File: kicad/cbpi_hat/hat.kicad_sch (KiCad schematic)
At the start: 26 parts, among them J1 GPIO, J2 Screw_Terminal_01x02, U1 CAT24C256, U2 EUP3453WIR1

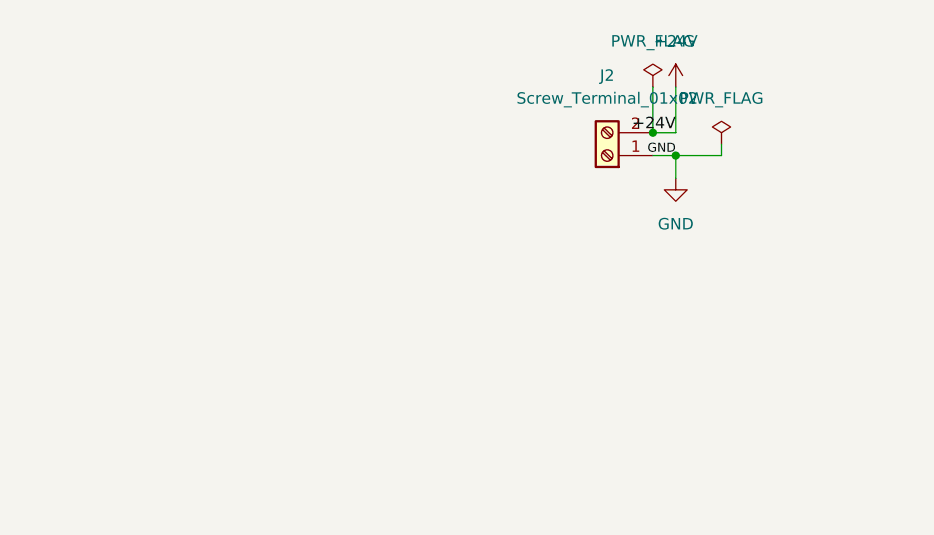
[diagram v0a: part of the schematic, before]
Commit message: The schematic should now have the current reverse polarity proection
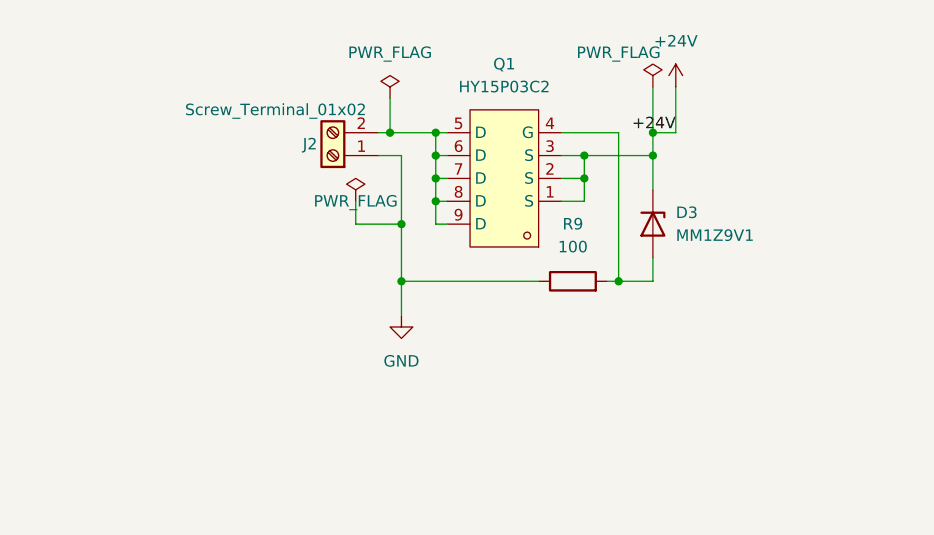
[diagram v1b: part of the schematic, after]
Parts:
- added D3: MM1Z9V1, symbol Device:D_Zener
- added Q1: HY15P03C2, hy15p03c2:DFN-8_L5.9-W5.2-P1.27-LS6.2-BL, symbol hy15p03c2:HY15P03C2
- added R9: 100, symbol Device:R
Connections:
- net +24V: now also D3.1 (K), Q1.1 (S), Q1.2 (S), Q1.3 (S); no longer J2.2 (Pin_2)
- net GND: now also R9.1
- new net: D3.2 (A), Q1.4 (G), R9.2
- new net: J2.2 (Pin_2), Q1.5 (D), Q1.6 (D), Q1.7 (D), Q1.8 (D), Q1.9 (D)
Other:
- moved on the sheet: J2

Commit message: Placed first components on board, no routing yet
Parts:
- D1: footprint Diode_SMD:D_SMC -> Diode_SMD:D_SMA
- D2: footprint smbj5:SMB_L4.6-W3.6-LS5.3-BI -> smbj5.0ca-tp:SMB_L4.6-W3.6-LS5.3-BI
- D3: footprint (none) -> Diode_SMD:D_SOD-123
- J2: footprint (none) -> TerminalBlock:TerminalBlock_Altech_AK300-2_P5.00mm
- R9: footprint (none) -> Resistor_SMD:R_01005_0402Metric
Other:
- note added: "Power In/ Reverse Polarity Protection"
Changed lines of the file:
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@@
+    (stroke (width 0) (type default) (color 0 0 0 0))
+  )
+  (polyline (pts (xy 292.1 12.7) (xy 292.1 53.34))
     (stroke (width 0) (type default) (color 0 0 0 0))
   )
@@
     (stroke (width 0) (type solid) (color 0 0 0 0))
   )
+  (polyline (pts (xy 359.41 12.7) (xy 359.41 53.34))
+    (stroke (width 0) (type default) (color 0 0 0 0))
+  )
   (wire (pts (xy 538.48 48.26) (xy 543.56 48.26))
     (stroke (width 0) (type default) (color 0 0 0 0))
@@
     (stroke (width 0) (type default) (color 0 0 0 0))
   )
+  (polyline (pts (xy 292.1 12.7) (xy 359.41 12.7))
+    (stroke (width 0) (type default) (color 0 0 0 0))
+  )
   (wire (pts (xy 346.71 20.32) (xy 346.71 25.4))
     (stroke (width 0) (type default) (color 0 0 0 0))
@@
   (wire (pts (xy 81.28 187.96) (xy 81.28 190.5))
     (stroke (width 0) (type solid) (color 0 0 0 0))
+  )
+  (polyline (pts (xy 359.41 53.34) (xy 292.1 53.34))
+    (stroke (width 0) (type default) (color 0 0 0 0))
   )
   (wire (pts (xy 476.25 29.21) (xy 469.9 29.21))
@@
   )
   (text "RPi Power Supply +5V" (at 576.58 22.86 180)
+    (effects (font (size 1.27 1.27)) (justify right bottom))
+  )
+  (text "Power In/\nReverse Polarity Protection" (at 358.14 52.07 180)
     (effects (font (size 1.27 1.27)) (justify right bottom))
   )
@@
     (property "Reference" "R9" (id 0) (at 337.82 35.56 90))
     (property "Value" "100" (id 1) (at 337.82 38.1 90))
-    (property "Footprint" "" (id 2) (at 337.82 43.688 90)
+    (property "Footprint" "Resistor_SMD:R_01005_0402Metric" (id 2) (at 337.82 43.688 90)
       (effects (font (size 1.27 1.27)) hide)
     )
@@
       (effects (font (size 1.27 1.27)) (justify left))
     )
-    (property "Footprint" "" (id 2) (at 346.71 35.56 0)
+    (property "Footprint" "Diode_SMD:D_SOD-123" (id 2) (at 346.71 35.56 0)
       (effects (font (size 1.27 1.27)) hide)
     )
@@
       (effects (font (size 1.27 1.27)) (justify left))
     )
-    (property "Footprint" "Diode_SMD:D_SMC" (id 2) (at 418.465 40.64 0)
+    (property "Footprint" "Diode_SMD:D_SMA" (id 2) (at 418.465 40.64 0)
       (effects (font (size 1.27 1.27)) hide)
     )
@@
       (effects (font (size 1.27 1.27)) (justify right))
     )
-    (property "Footprint" "smbj5:SMB_L4.6-W3.6-LS5.3-BI" (id 2) (at 557.53 57.15 0)
+    (property "Footprint" "smbj5.0ca-tp:SMB_L4.6-W3.6-LS5.3-BI" (id 2) (at 557.53 57.15 0)
       (effects (font (size 1.27 1.27)) hide)
     )
@@
     (property "Reference" "J2" (id 0) (at 308.61 26.67 0))
     (property "Value" "Screw_Terminal_01x02" (id 1) (at 304.8 22.86 0))
-    (property "Footprint" "" (id 2) (at 311.15 27.94 0)
+    (property "Footprint" "TerminalBlock:TerminalBlock_Altech_AK300-2_P5.00mm" (id 2) (at 311.15 27.94 0)
       (effects (font (size 1.27 1.27)) hide)
     )
@@
     )
     (path "/95466bc2-2f9a-4e01-98ff-50b74edc683e"
-      (reference "D1") (unit 1) (value "B340") (footprint "Diode_SMD:D_SMC")
+      (reference "D1") (unit 1) (value "B340") (footprint "Diode_SMD:D_SMA")
     )
     (path "/e09c61c5-f879-4d7b-9aea-65e05039ac50"
-      (reference "D2") (unit 1) (value "SMBJ5.0CA-TP") (footprint "smbj5:SMB_L4.6-W3.6-LS5.3-BI")
+      (reference "D2") (unit 1) (value "SMBJ5.0CA-TP") (footprint "smbj5.0ca-tp:SMB_L4.6-W3.6-LS5.3-BI")
     )
     (path "/336f2b08-bcb1-4a5f-b6b3-a07ce6682305"
-      (reference "D3") (unit 1) (value "MM1Z9V1") (footprint "")
+      (reference "D3") (unit 1) (value "MM1Z9V1") (footprint "Diode_SMD:D_SOD-123")
     )
     (path "/00000000-0000-0000-0000-000059ad464a"
@@
     )
     (path "/eb295de6-9c43-4209-a110-446145aec0d0"
-      (reference "J2") (unit 1) (value "Screw_Terminal_01x02") (footprint "")
+      (reference "J2") (unit 1) (value "Screw_Terminal_01x02") (footprint "TerminalBlock:TerminalBlock_Altech_AK300-2_P5.00mm")
     )
     (path "/43e66c4c-de75-44f8-8171-19825b035cbb"
@@
     )
     (path "/02425376-84d4-4278-bf84-70f0e0df41cc"
-      (reference "R9") (unit 1) (value "100") (footprint "")
+      (reference "R9") (unit 1) (value "100") (footprint "Resistor_SMD:R_01005_0402Metric")
     )
     (path "/6d6e5c8e-c0cf-4e61-9c00-723a754d58be"
